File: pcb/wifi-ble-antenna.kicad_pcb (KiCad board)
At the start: 4 copper layers, 41.3 x 42.5 mm, 6 parts, among them J1 BWSMA-KE-P001

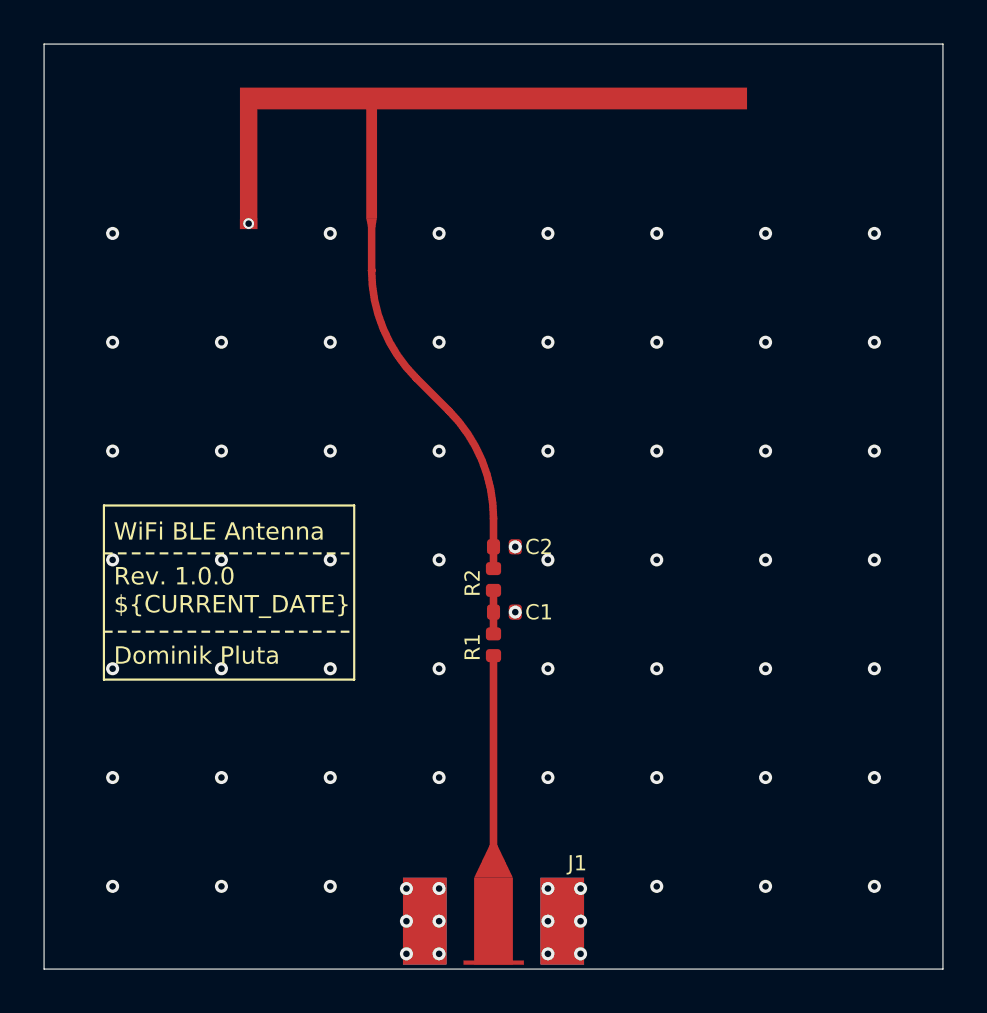
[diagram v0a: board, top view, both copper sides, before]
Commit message: PCB: Move matching network closer to the antenna element
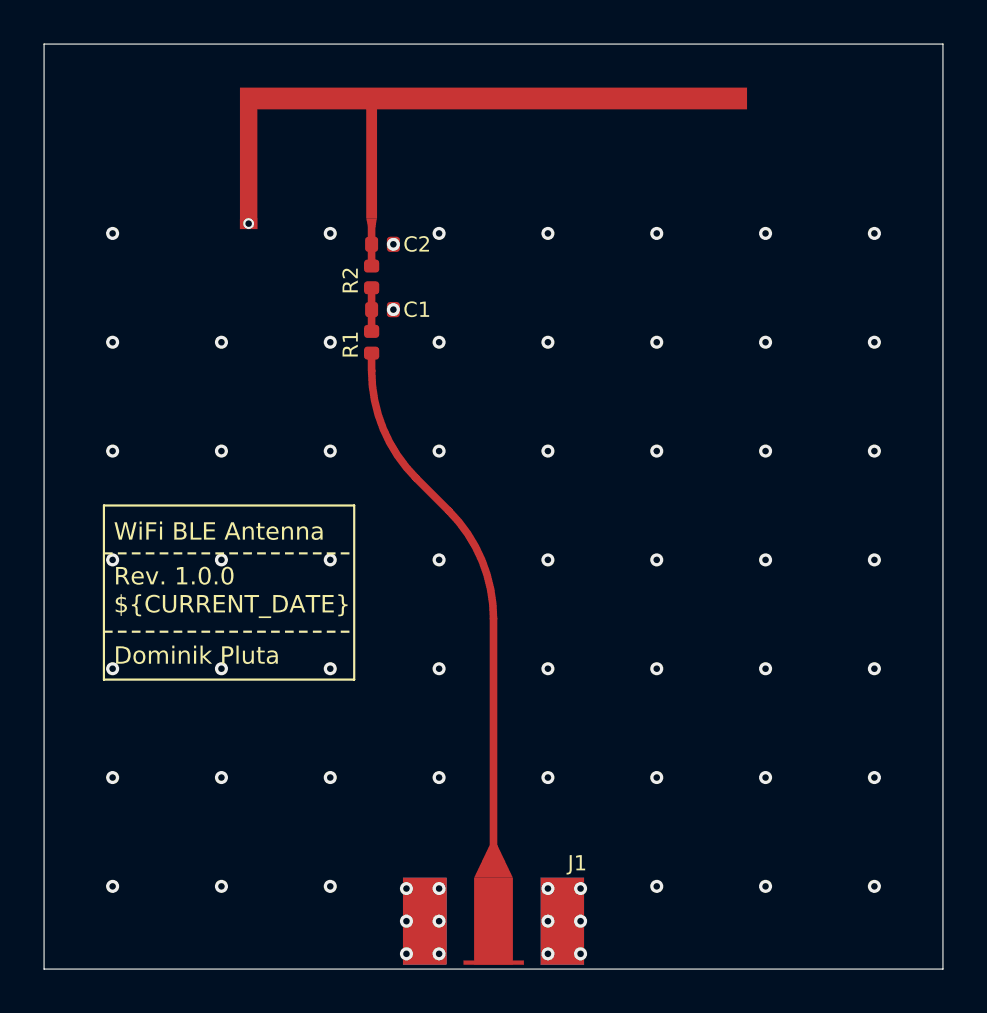
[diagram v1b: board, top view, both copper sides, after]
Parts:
- moved C1 15.0 mm to (144.9, 92.2)
- moved C2 15.0 mm to (144.9, 89.2)
- moved R1 15.0 mm to (144.4, 93.7)
- moved R2 15.0 mm to (144.4, 90.7)
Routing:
- net Net-(J1-Pad1): track 9.70 -> 25.2 mm
- net Net-(E1-SIG): track 17.5 -> 1.95 mm
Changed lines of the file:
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@@
 	(footprint "DW-footprints:C_0402_1005Metric"
 		(layer "F.Cu")
-		(at 150.5 106.1 180)
+		(at 144.9 92.2 180)
 		(descr "Capacitor SMD 0402")
 		(tags "capacitor SMD 0402")
@@
 	(footprint "DW-footprints:R_0402_1005Metric"
 		(layer "F.Cu")
-		(at 150 104.6 90)
+		(at 144.4 90.7 90)
 		(descr "Resistor SMD 0402")
 		(tags "resistor SMD 0402")
@@
 	(footprint "DW-footprints:C_0402_1005Metric"
 		(layer "F.Cu")
-		(at 150.5 103.1 180)
+		(at 144.9 89.2 180)
 		(descr "Capacitor SMD 0402")
 		(tags "capacitor SMD 0402")
@@
 	(footprint "DW-footprints:R_0402_1005Metric"
 		(layer "F.Cu")
-		(at 150 107.6 90)
+		(at 144.4 93.7 90)
 		(descr "Resistor SMD 0402")
 		(tags "resistor SMD 0402")
@@
 	)
 	(via
-		(at 151 103.1)
+		(at 145.4 89.2)
 		(size 0.6)
 		(drill 0.3)
@@
 	)
 	(via
-		(at 151 106.1)
+		(at 145.4 92.2)
 		(size 0.6)
 		(drill 0.3)
@@
 	)
 	(segment
-		(start 150.000001 106.1)
-		(end 150.000001 105.1)
+		(start 144.4 92.200001)
+		(end 144.400001 92.2)
 		(width 0.3493)
 		(layer "F.Cu")
@@
 	)
 	(segment
-		(start 150 107.100001)
-		(end 150 106.100001)
+		(start 144.4 91.199999)
+		(end 144.4 92.199999)
 		(width 0.3493)
 		(layer "F.Cu")
@@
 	)
 	(segment
-		(start 150.000001 105.1)
-		(end 150 105.099999)
+		(start 144.4 92.199999)
+		(end 144.400001 92.2)
 		(width 0.3493)
 		(layer "F.Cu")
@@
 	)
 	(segment
-		(start 150 106.100001)
-		(end 150.000001 106.1)
+		(start 144.4 93.200001)
+		(end 144.4 92.200001)
 		(width 0.3493)
 		(layer "F.Cu")
@@
 	)
 	(segment
-		(start 144.4 90.400505)
-		(end 144.400453 90.400052)
-		(width 0.3493)
-		(layer "F.Cu")
-		(net 3)
-	)
-	(segment
-		(start 147.949748 96.849748)
-		(end 146.450252 95.350252)
-		(width 0.3493)
-		(layer "F.Cu")
-		(net 3)
-	)
-	(segment
-		(start 150 104.1)
-		(end 150.000001 103.1)
-		(width 0.3493)
-		(layer "F.Cu")
-		(net 3)
-	)
-	(segment
-		(start 144.400453 90.400052)
-		(end 144.400453 88.250453)
+		(start 144.400001 90.2)
+		(end 144.4 90.200001)
 		(width 0.3493)
 		(layer "F.Cu")
@@
 	)
 	(segment
-		(start 150.000001 103.1)
-		(end 150.000001 101.799497)
+		(start 144.400001 88.250001)
+		(end 144.4 88.25)
 		(width 0.3493)
 		(layer "F.Cu")
 		(net 3)
 	)
-	(arc
-		(start 146.450252 95.350252)
-		(mid 144.932843 93.079289)
-		(end 144.4 90.400505)
+	(segment
+		(start 144.400001 89.2)
+		(end 144.400001 90.2)
 		(width 0.3493)
 		(layer "F.Cu")
 		(net 3)
 	)
-	(arc
-		(start 150.000001 101.799496)
-		(mid 149.467158 99.120712)
-		(end 147.949748 96.849748)
+	(segment
+		(start 144.400001 89.2)
+		(end 144.400001 88.250001)
 		(width 0.3493)
 		(layer "F.Cu")
@@
 	)
 	(segment
-		(start 150 117.799999)
-		(end 150 108.099998)
+		(start 146.450253 99.950253)
+		(end 147.949748 101.449748)
+		(width 0.3493)
+		(layer "F.Cu")
+		(net 4)
+	)
+	(segment
+		(start 144.4 94.199999)
+		(end 144.4 95.000505)
+		(width 0.3493)
+		(layer "F.Cu")
+		(net 4)
+	)
+	(segment
+		(start 150 106.399495)
+		(end 150 117.799999)
 		(width 0.3493)
 		(layer "F.Cu")
@@
 		(width 0.3493)
 		(layer "F.Cu")
+		(net 4)
+	)
+	(arc
+		(start 146.450253 99.950253)
+		(mid 144.932843 97.679289)
+		(end 144.4 95.000505)
+		(width 0.3493)
+		(layer "F.Cu")
+		(net 4)
+	)
+	(arc
+		(start 147.949748 101.449748)
+		(mid 149.467157 103.720711)
+		(end 150 106.399495)
+		(width 0.3493)
+		(layer "F.Cu")
